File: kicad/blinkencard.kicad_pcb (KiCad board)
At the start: 2 copper layers, 88.9 x 50.8 mm, 100 parts, among them J1 USB_B_Micro, Q1 BC847, Q2 BC847, Q3 BC847, Q4 BC847, Q5 BC847, SW1 0, SW2 1, SW3 LEFT, SW4 RIGHT, U1 ICE40UP5K-SG48ITR, U2 W25Q64JV, U3 CP2102N-A01-GQFN28, U4 MIC5504-1.2YM5, U5 MIC5504-3.3YM5

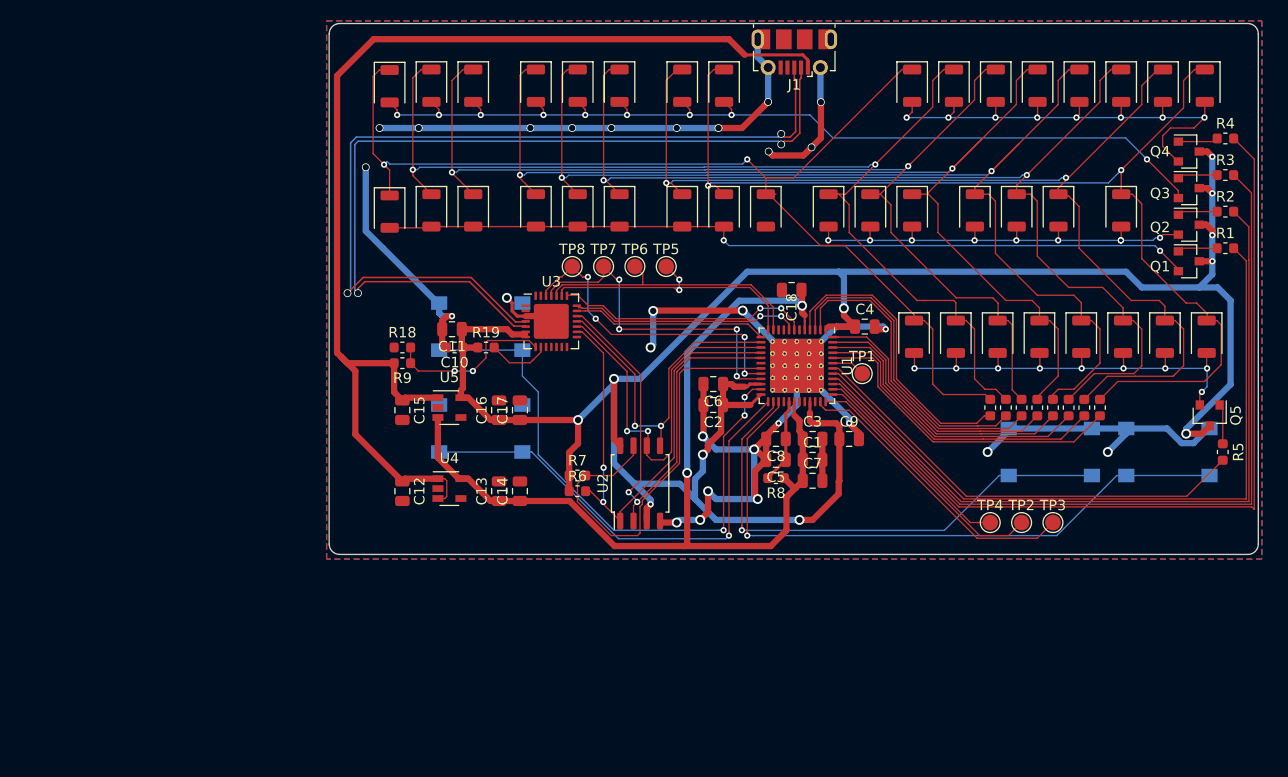
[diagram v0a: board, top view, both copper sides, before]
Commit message: Routing complete. DRC passes. Need to fix silk around LEDs and do final check
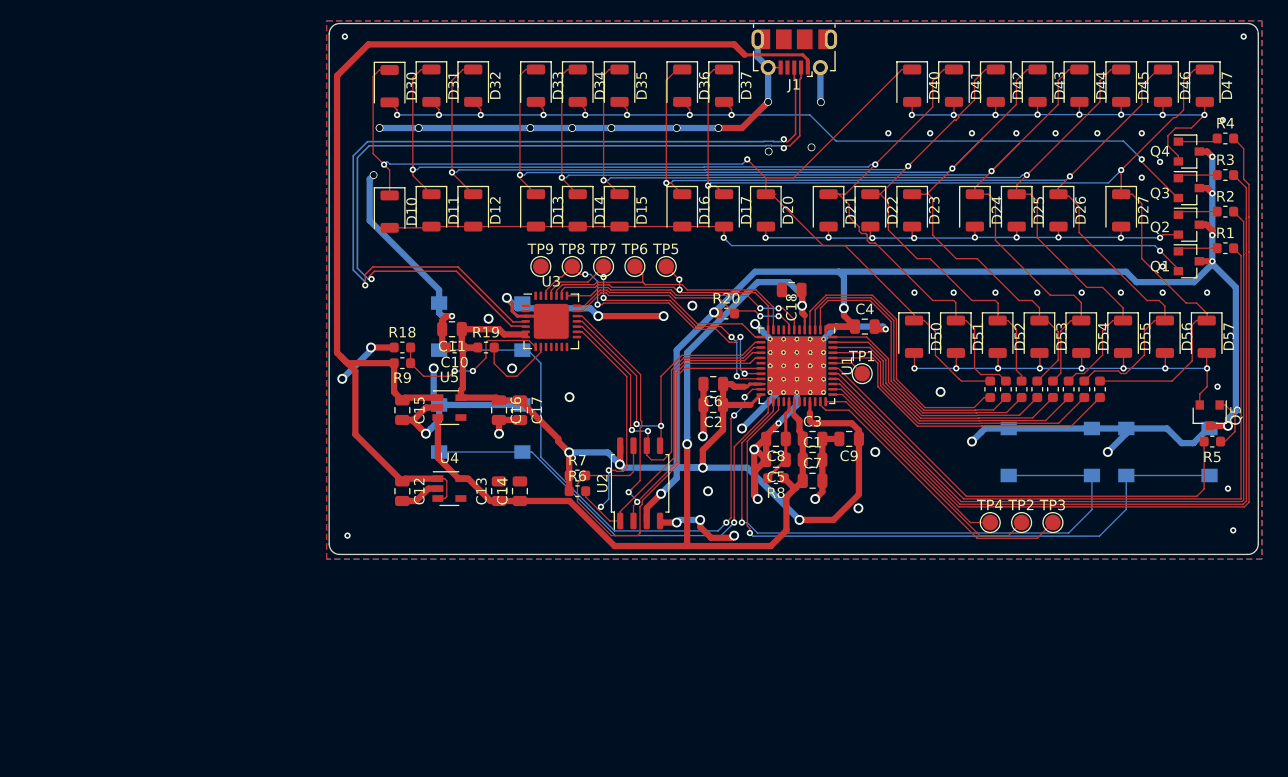
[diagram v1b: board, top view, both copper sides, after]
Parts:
- added R20: 10K, Resistor_SMD:R_0603_1608Metric, F.Cu at (38.0, 27.8)
- added TP9: GND, TestPoint:TestPoint_Pad_D1.5mm, F.Cu at (20.2, 23.2)
- U1: footprint Package_DFN_QFN:QFN-48-1EP_7x7mm_P0.5mm_EP5.15x5.15mm_ThermalVias -> Package_DFN_QFN:QFN-48-1EP_7x7mm_P0.5mm_EP5.6x5.6mm_ThermalVias
- moved R10 1.75 mm to (63.2, 35.0)
- moved R11 1.75 mm to (64.8, 35.0)
- moved R12 1.75 mm to (66.2, 35.0)
- moved R13 1.75 mm to (67.8, 35.0)
- moved R14 1.75 mm to (69.2, 35.0)
- moved R15 1.75 mm to (70.8, 35.0)
- moved R16 1.75 mm to (72.2, 35.0)
- moved R17 1.75 mm to (73.8, 35.0)
- moved R5 1.41 mm to (84.5, 40.0), turned to 180 degrees
- turned C16 to 270 degrees
- turned C17 to 270 degrees
- turned C9 to 180 degrees
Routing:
- net GND: track 194.7 -> 223.6 mm, vias 28 -> 67
- net VDD: track 223.4 -> 213.5 mm, vias 11 -> 12
- net BUTTON_R: track 49.2 -> 58.9 mm
- net Net-(D15-Pad1): track 104.2 -> 98.1 mm
- net Net-(D20-Pad2): track 43.1 -> 48.4 mm
- net Net-(D16-Pad1): track 103.7 -> 98.4 mm
- net Net-(D14-Pad1): track 106.6 -> 101.8 mm
- net FPGA_SS: track 47.9 -> 51.7 mm
- net Net-(D40-Pad2): track 48.9 -> 45.2 mm
- net Net-(D17-Pad1): track 105.2 -> 101.6 mm
- net Net-(D10-Pad1): track 105.4 -> 102.9 mm
- net /usb_and_power/D-: track 82.5 -> 80.0 mm
- net FPGA_TXO: track 32.0 -> 29.6 mm
- net +1V2: track 91.9 -> 94.0 mm
- net Net-(R19-Pad2): track 5.99 -> 7.95 mm
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
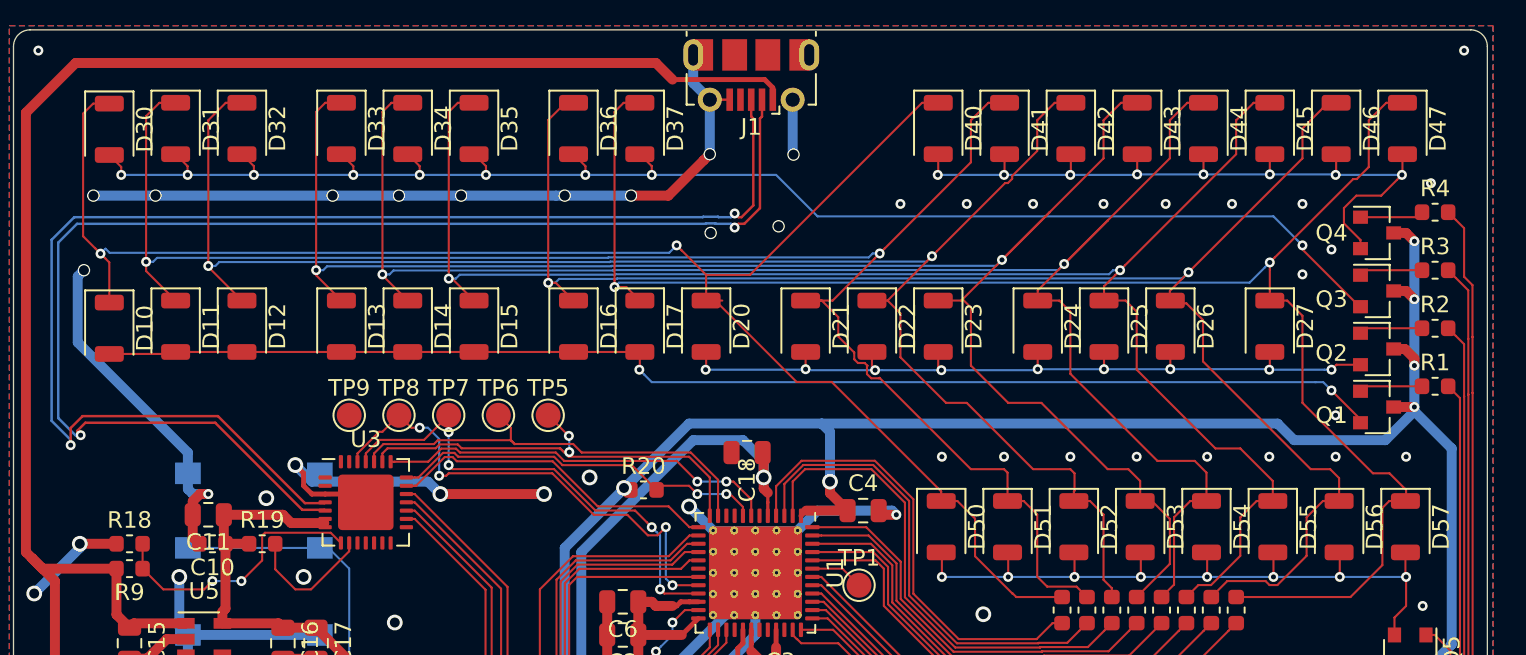
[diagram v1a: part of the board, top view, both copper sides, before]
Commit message: Fix LED silk, minor routing cleanups
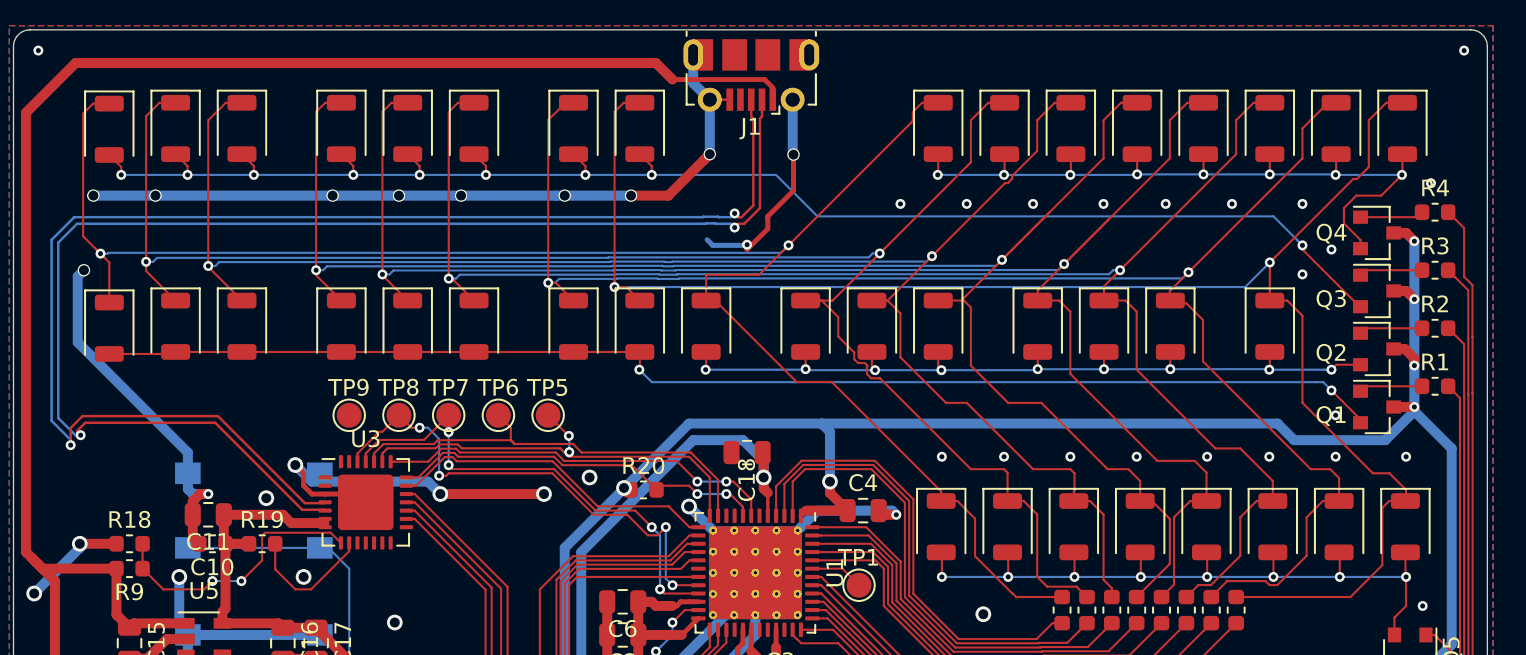
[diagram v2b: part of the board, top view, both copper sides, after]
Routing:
- net GND: track 223.6 -> 233.4 mm, vias 67 -> 66
- net Net-(D10-Pad1): track 102.9 -> 106.7 mm
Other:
- board text added: "A0"
- board text added: "A1"
- board text added: "A10"
- board text added: "A11"
- board text added: "A12"
- board text added: "A13"
- board text added: "A14"
- board text added: "A15"
- board text added: "A2"
- board text added: "A3"
- board text added: "A4"
- board text added: "A5"
- board text added: "A6"
- board text added: "A7"
- board text added: "A8"
- board text added: "A9"
- board text added: "AUX0"
- board text added: "AUX1"
- board text added: "AUX2"
- board text added: "D0"
- board text added: "D1"
- board text added: "D2"
- board text added: "D3"
- board text added: "D4"
- board text added: "D5"
- board text added: "D6"
- board text added: "D7"
- board text added: "HLDA"
- board text added: "HLTA"
- board text added: "INP"
- board text added: "INT"
- board text added: "INTE"
- board text added: "MEMR"
- board text added: "MI"
- board text added: "OUT"
- board text added: "RUN"
- board text added: "STACK"
- board text added: "WAIT"
- board text added: "WO"

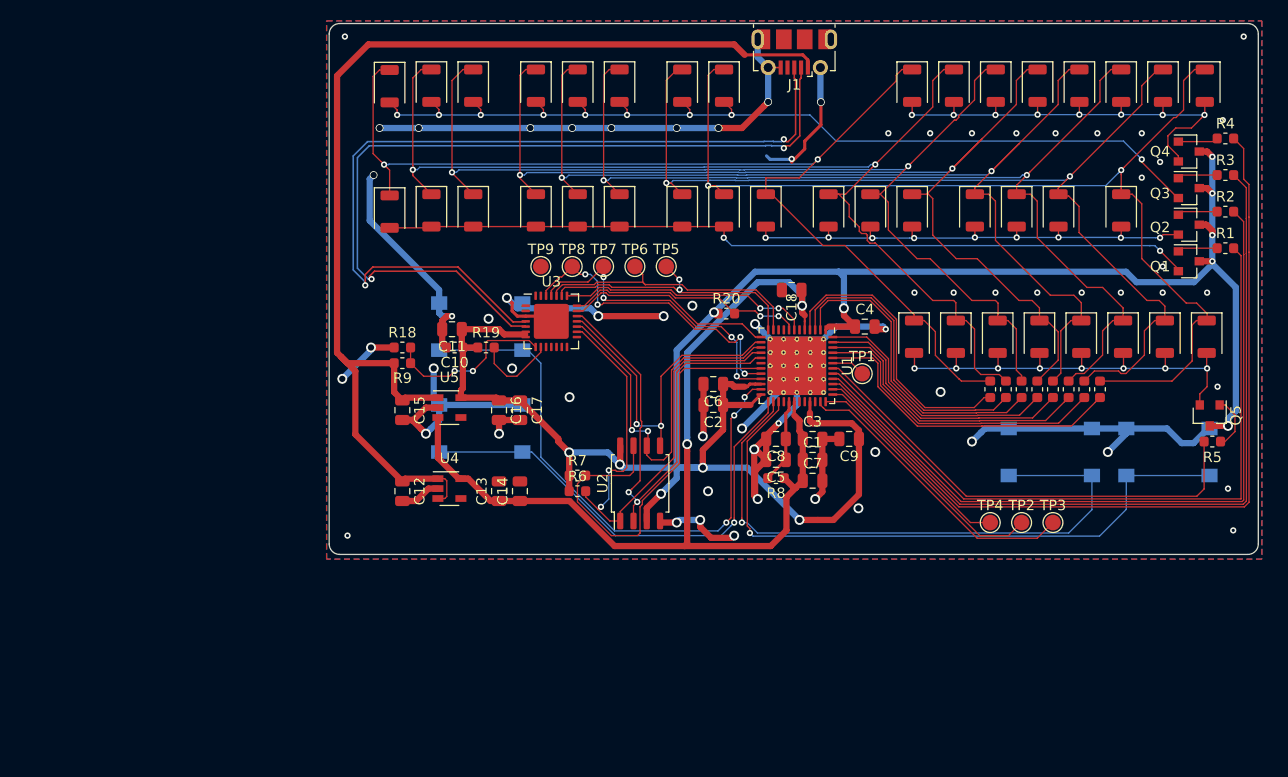
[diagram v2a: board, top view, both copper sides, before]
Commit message: Refdes silk placement, label cleanup, ground via cleanup
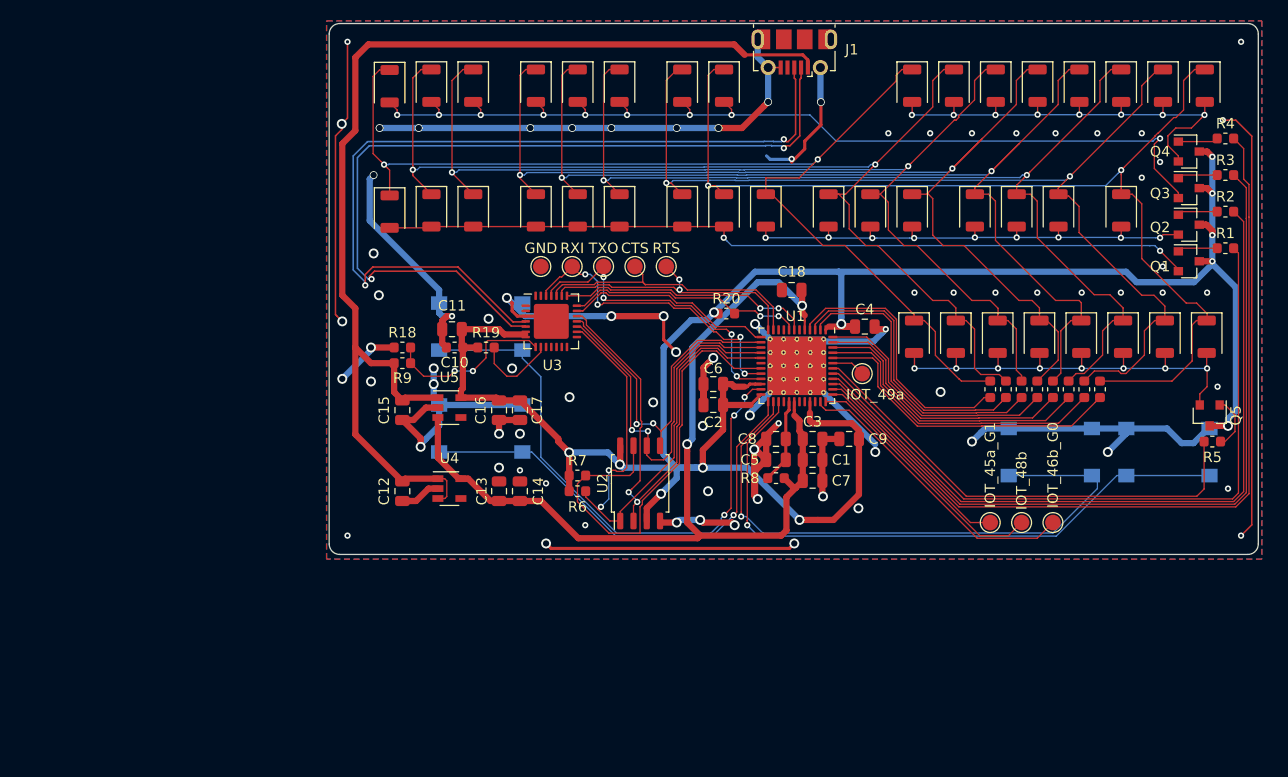
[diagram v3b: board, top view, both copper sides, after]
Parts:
- TP5: value FPGA_RTS -> RTS
- TP6: value FPGA_CTS -> CTS
- TP7: value FPGA_TXO -> TXO
- TP8: value FPGA_RXI -> RXI
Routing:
- net GND: track 233.4 -> 336.2 mm, vias 66 -> 81
- net VDD: track 213.5 -> 217.1 mm
- net Net-(D30-Pad2): track 90.5 -> 93.4 mm
- net BUTTON_L: track 62.3 -> 60.1 mm
- net LED_COL_2: track 30.0 -> 28.1 mm
- net LED_COL_1: track 28.9 -> 27.1 mm
- net +1V2: track 94.0 -> 92.2 mm
- net LED_COL_0: track 27.9 -> 26.1 mm
- net +5V: track 108.7 -> 107.2 mm
- net FLASH_HOLDn: track 42.8 -> 43.9 mm
- net BUTTON_R: track 58.9 -> 57.7 mm
- net FPGA_SI_FLASH_MISO: track 46.1 -> 46.8 mm
- net LED_ROW_0: track 68.3 -> 67.6 mm
- net FPGA_SO_FLASH_MOSI: track 32.5 -> 33.1 mm
- net FPGA_SS: track 51.7 -> 52.2 mm

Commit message: Move buttons to more sensible locations, finalize silk, tape out v1.0
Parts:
- moved SW2 7.75 mm to (14.2, 36.8)
- moved SW1 6.50 mm to (14.2, 45.2)
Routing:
- net BUTTON_1: track 54.4 -> 48.6 mm
- net Net-(R19-Pad2): track 7.95 -> 5.40 mm
- net BUTTON_0: track 44.5 -> 42.2 mm
- net GND: track 336.2 -> 338.0 mm, vias 81 -> 77
- net Net-(R18-Pad2): track 16.5 -> 15.8 mm
- net FPGA_SS: track 52.2 -> 51.6 mm
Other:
- board text added: "Blinkencard"
- board text added: "v1.0 11/19 by Andrew Litt https://github.com/al177/blinkencard"

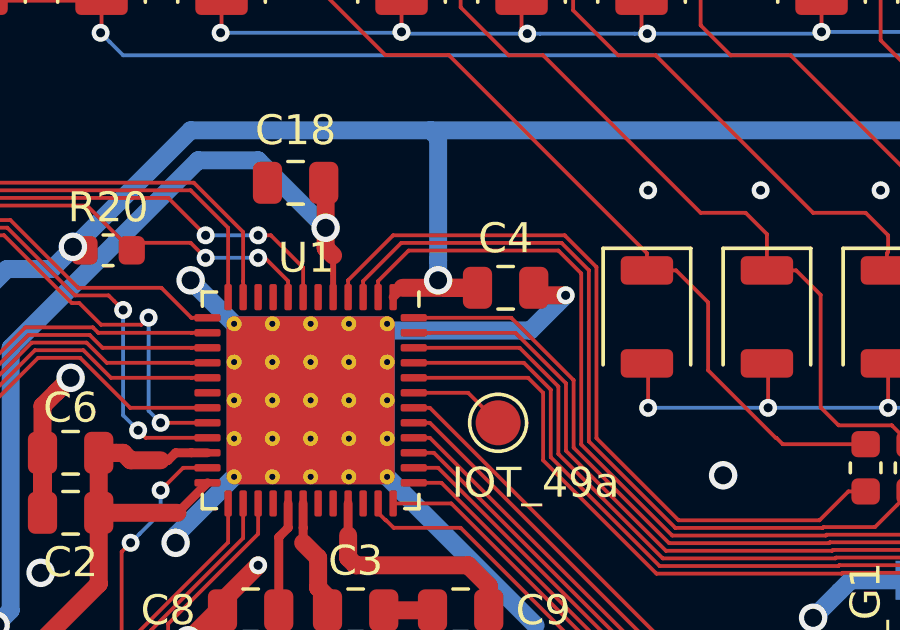
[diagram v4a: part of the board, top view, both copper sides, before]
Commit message: Fix minor ground plane issue before submitting v1.0
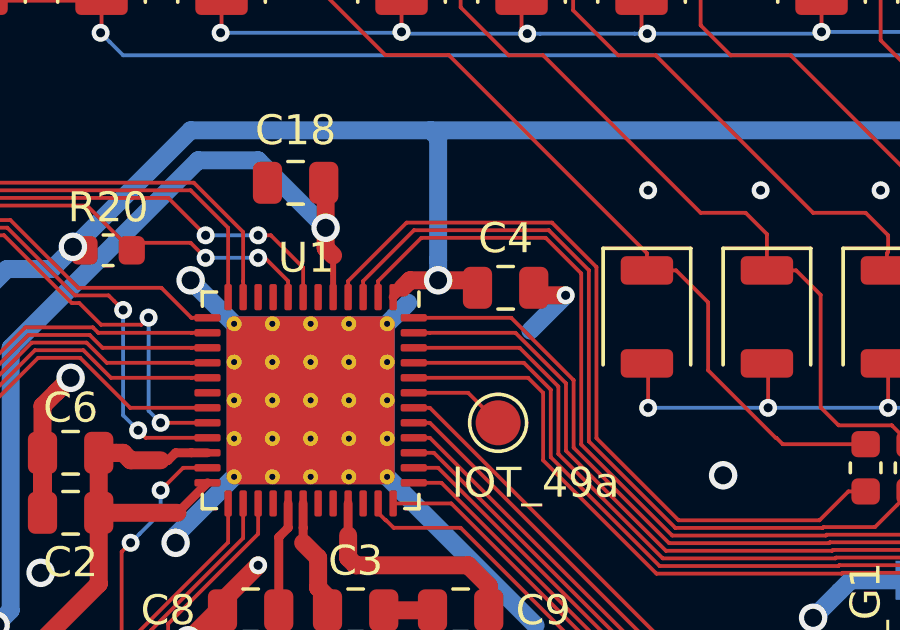
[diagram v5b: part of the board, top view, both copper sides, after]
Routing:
- net VDD: track 217.6 -> 216.4 mm
